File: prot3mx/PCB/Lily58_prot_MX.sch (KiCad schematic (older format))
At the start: 94 parts, among them J1 LED, J2 4PIN, J3 OLED, P1 i2c_pin, P2 i2c_pin, SW1 SW_PUSH, SW10 SW_PUSH, SW11 SW_PUSH, SW12 SW_PUSH, SW13 SW_PUSH, SW14 SW_PUSH, SW15 SW_PUSH, SW16 SW_PUSH, SW17 SW_PUSH, SW18 SW_PUSH, SW19 SW_PUSH, SW2 SW_PUSH, SW20 SW_PUSH, SW21 SW_PUSH, SW22 SW_PUSH, SW23 SW_PUSH, SW24 SW_PUSH, SW25 SW_PUSH, SW26 SW_PUSH, SW27 SW_PUSH, SW28 SW_PUSH, SW29 SW_PUSH, SW3 SW_PUSH, SW30 ROT_ENC_SW, SW31 ROT_ENC_SW, SW32 ROT_ENC_SW, SW4 SW_PUSH, SW5 SW_PUSH, SW6 SW_PUSH, SW7 SW_PUSH, SW8 SW_PUSH, SW9 SW_PUSH, U1 ProMicro

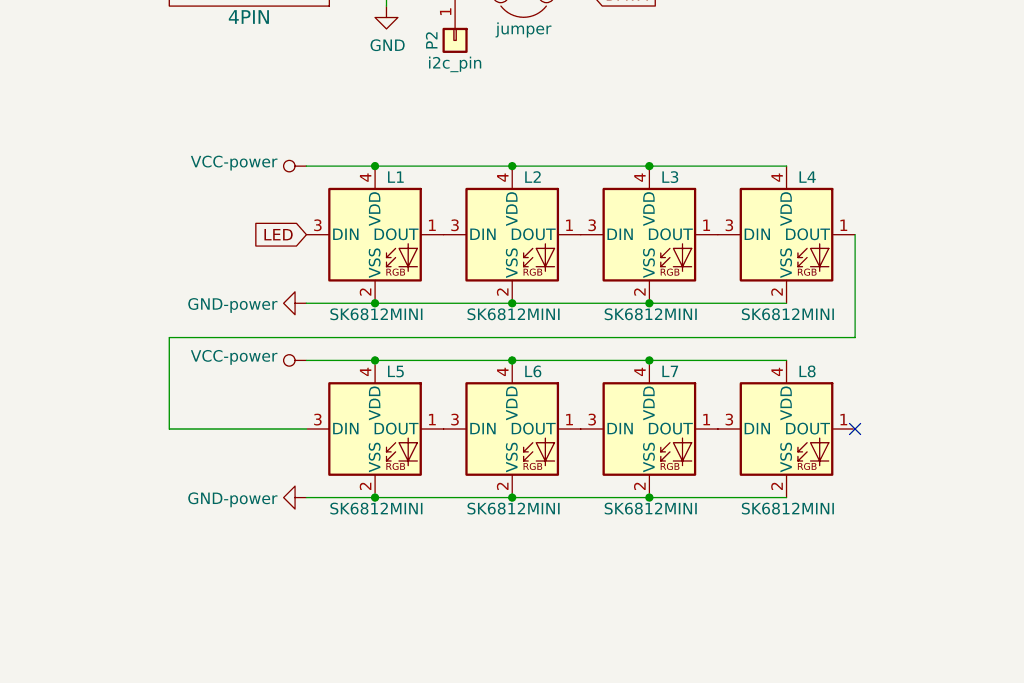
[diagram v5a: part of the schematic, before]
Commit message: keeping only 1 LED as indicator and fixed all remaining unconnected traces
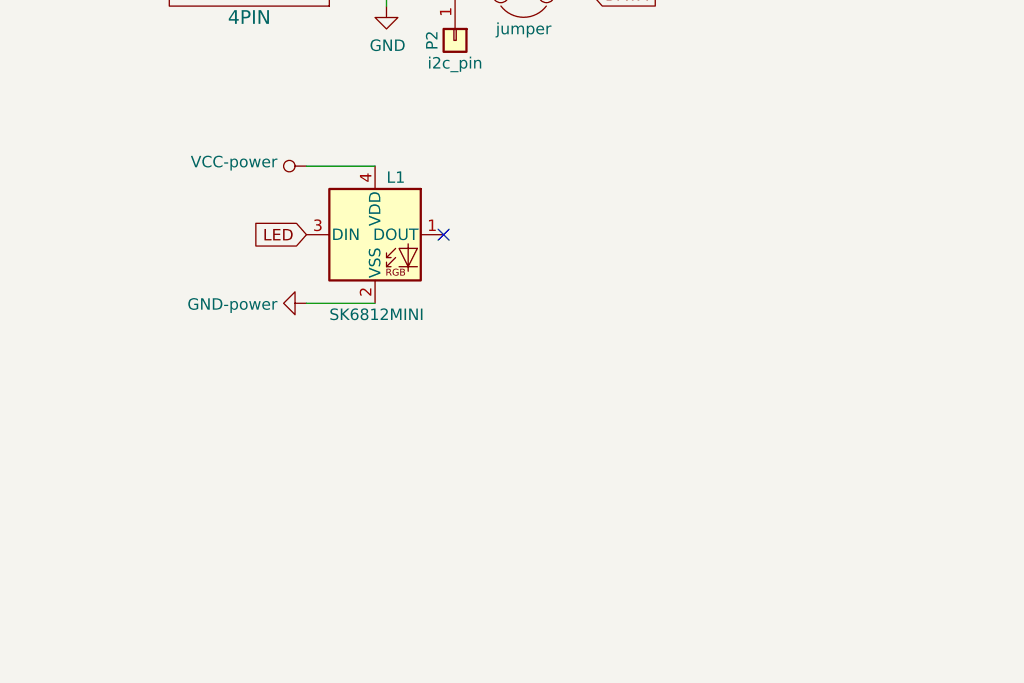
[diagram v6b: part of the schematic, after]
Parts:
- removed L2, L3, L4, L5, L6, L7, L8: SK6812MINI, Lily58_prot_MX-footprint:SK6812MINI_underglow_rev, symbol Lily58_prot_MX-rescue:LED_SK6812MINI
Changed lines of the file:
@@
 	0    1    1    0
 $EndComp
-Connection ~ 2600 3350
-Connection ~ 2600 3950
-$Comp
-L Lily58_prot_MX-rescue:VCC-power #PWR0108
-U 1 1 5FFDCA85
-P 2300 4200
-F 0 "#PWR0108" H 2300 4050 50  0001 C CNN
-F 1 "VCC-power" V 2318 4327 50  0000 L CNN
-F 2 "" H 2300 4200 50  0001 C CNN
-F 3 "" H 2300 4200 50  0001 C CNN
-	1    2300 4200
-	0    -1   -1   0
-$EndComp
-$Comp
-L Lily58_prot_MX-rescue:GND-power #PWR0109
-U 1 1 5FFDCA8F
-P 2300 4800
-F 0 "#PWR0109" H 2300 4550 50  0001 C CNN
-F 1 "GND-power" V 2305 4673 50  0000 R CNN
-F 2 "" H 2300 4800 50  0001 C CNN
-F 3 "" H 2300 4800 50  0001 C CNN
-	1    2300 4800
-	0    1    1    0
-$EndComp
-Wire Wire Line
-	1700 4500 2300 4500
 Wire Wire Line
 	6800 3300 6950 3300
@@
 	10150 3300 10150 3550
 Connection ~ 10150 3550
-Wire Wire Line
-	1700 4100 1700 4500
-Wire Wire Line
-	2600 3950 3200 3950
-Wire Wire Line
-	2600 3350 3200 3350
-$Comp
-L Lily58_prot_MX-rescue:LED_SK6812MINI L2
-U 1 1 5FF372B2
-P 3200 3650
-F 0 "L2" H 3250 3900 50  0000 L CNN
-F 1 "SK6812MINI" H 3000 3300 50  0000 L CNN
-F 2 "Lily58_prot_MX-footprint:SK6812MINI_underglow_rev" H 3250 3350 50  0001 L TNN
-F 3 "" H 3300 3275 50  0001 L TNN
-	1    3200 3650
-	1    0    0    -1
-$EndComp
-Connection ~ 3200 3950
-Wire Wire Line
-	3200 3950 3800 3950
-Connection ~ 3200 3350
-Wire Wire Line
-	3200 3350 3800 3350
-$Comp
-L Lily58_prot_MX-rescue:LED_SK6812MINI L3
-U 1 1 5FF388C3
-P 3800 3650
-F 0 "L3" H 3850 3900 50  0000 L CNN
-F 1 "SK6812MINI" H 3600 3300 50  0000 L CNN
-F 2 "Lily58_prot_MX-footprint:SK6812MINI_underglow_rev" H 3850 3350 50  0001 L TNN
-F 3 "" H 3900 3275 50  0001 L TNN
-	1    3800 3650
-	1    0    0    -1
-$EndComp
-Wire Wire Line
-	2300 4800 2600 4800
-Wire Wire Line
-	2300 4200 2600 4200
-$Comp
-L Lily58_prot_MX-rescue:LED_SK6812MINI L5
-U 1 1 5FF55256
-P 2600 4500
-F 0 "L5" H 2650 4750 50  0000 L CNN
-F 1 "SK6812MINI" H 2400 4150 50  0000 L CNN
-F 2 "Lily58_prot_MX-footprint:SK6812MINI_underglow_rev" H 2650 4200 50  0001 L TNN
-F 3 "" H 2700 4125 50  0001 L TNN
-	1    2600 4500
-	1    0    0    -1
-$EndComp
-$Comp
-L Lily58_prot_MX-rescue:LED_SK6812MINI L6
-U 1 1 5FF55D14
-P 3200 4500
-F 0 "L6" H 3250 4750 50  0000 L CNN
-F 1 "SK6812MINI" H 3000 4150 50  0000 L CNN
-F 2 "Lily58_prot_MX-footprint:SK6812MINI_underglow_rev" H 3250 4200 50  0001 L TNN
-F 3 "" H 3300 4125 50  0001 L TNN
-	1    3200 4500
-	1    0    0    -1
-$EndComp
-$Comp
-L Lily58_prot_MX-rescue:LED_SK6812MINI L7
-U 1 1 5FF55D1E
-P 3800 4500
-F 0 "L7" H 3850 4750 50  0000 L CNN
-F 1 "SK6812MINI" H 3600 4150 50  0000 L CNN
-F 2 "Lily58_prot_MX-footprint:SK6812MINI_underglow_rev" H 3850 4200 50  0001 L TNN
-F 3 "" H 3900 4125 50  0001 L TNN
-	1    3800 4500
-	1    0    0    -1
-$EndComp
-Connection ~ 2600 4200
-Wire Wire Line
-	2600 4200 3200 4200
-Connection ~ 2600 4800
-Wire Wire Line
-	2600 4800 3200 4800
-Connection ~ 3200 4200
-Wire Wire Line
-	3200 4200 3800 4200
-Connection ~ 3200 4800
-Wire Wire Line
-	3200 4800 3800 4800
-Connection ~ 3800 4200
-Connection ~ 3800 4800
-Connection ~ 3800 3350
-Connection ~ 3800 3950
-Wire Wire Line
-	3800 4200 4400 4200
-Wire Wire Line
-	3800 4800 4400 4800
-$Comp
-L Lily58_prot_MX-rescue:LED_SK6812MINI L8
-U 1 1 5FF55D28
-P 4400 4500
-F 0 "L8" H 4450 4750 50  0000 L CNN
-F 1 "SK6812MINI" H 4200 4150 50  0000 L CNN
-F 2 "Lily58_prot_MX-footprint:SK6812MINI_underglow_rev" H 4450 4200 50  0001 L TNN
-F 3 "" H 4500 4125 50  0001 L TNN
-	1    4400 4500
-	1    0    0    -1
-$EndComp
-Wire Wire Line
-	3800 3350 4400 3350
-Wire Wire Line
-	3800 3950 4400 3950
-$Comp
-L Lily58_prot_MX-rescue:LED_SK6812MINI L4
-U 1 1 5FF39EEA
-P 4400 3650
-F 0 "L4" H 4450 3900 50  0000 L CNN
-F 1 "SK6812MINI" H 4200 3300 50  0000 L CNN
-F 2 "Lily58_prot_MX-footprint:SK6812MINI_underglow_rev" H 4450 3350 50  0001 L TNN
-F 3 "" H 4500 3275 50  0001 L TNN
-	1    4400 3650
-	1    0    0    -1
-$EndComp
-Wire Wire Line
-	1700 4100 4700 4100
-Wire Wire Line
-	4700 4100 4700 3650
-NoConn ~ 4700 4500
+NoConn ~ 2900 3650
 $EndSCHEMATC
